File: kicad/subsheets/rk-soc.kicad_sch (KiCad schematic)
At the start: 1 part, among them U4 RK3566

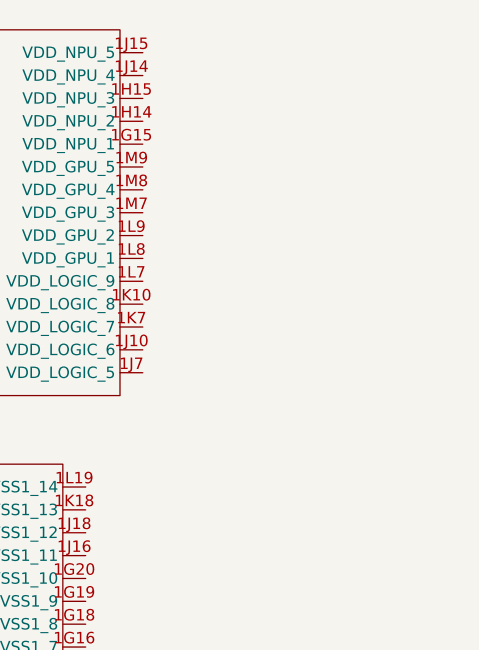
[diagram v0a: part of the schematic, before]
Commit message: Resize sheets
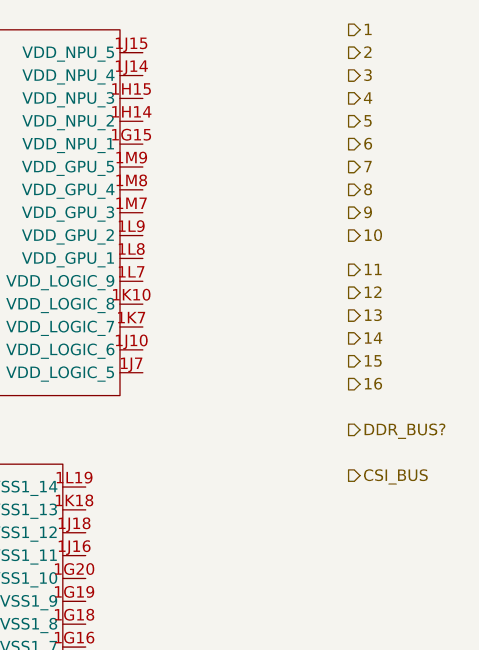
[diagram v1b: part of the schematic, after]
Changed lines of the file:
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@@
 	(generator_version "9.0")
 	(paper "A4")
+	(hierarchical_label "CSI_BUS"
+		(shape output)
+		(at 96.52 76.2 0)
+		(effects
+			(font
+				(size 1.27 1.27)
+			)
+			(justify left)
+		)
+	)
+	(hierarchical_label "16"
+		(shape output)
+		(at 96.52 66.04 0)
+		(effects
+			(font
+				(size 1.27 1.27)
+			)
+			(justify left)
+		)
+	)
+	(hierarchical_label "15"
+		(shape output)
+		(at 96.52 63.5 0)
+		(effects
+			(font
+				(size 1.27 1.27)
+			)
+			(justify left)
+		)
+	)
+	(hierarchical_label "10"
+		(shape output)
+		(at 96.52 49.53 0)
+		(effects
+			(font
+				(size 1.27 1.27)
+			)
+			(justify left)
+		)
+	)
+	(hierarchical_label "11"
+		(shape output)
+		(at 96.52 53.34 0)
+		(effects
+			(font
+				(size 1.27 1.27)
+			)
+			(justify left)
+		)
+	)
+	(hierarchical_label "12"
+		(shape output)
+		(at 96.52 55.88 0)
+		(effects
+			(font
+				(size 1.27 1.27)
+			)
+			(justify left)
+		)
+	)
+	(hierarchical_label "13"
+		(shape output)
+		(at 96.52 58.42 0)
+		(effects
+			(font
+				(size 1.27 1.27)
+			)
+			(justify left)
+		)
+	)
+	(hierarchical_label "14"
+		(shape output)
+		(at 96.52 60.96 0)
+		(effects
+			(font
+				(size 1.27 1.27)
+			)
+			(justify left)
+		)
+	)
+	(hierarchical_label "4"
+		(shape output)
+		(at 96.52 34.29 0)
+		(effects
+			(font
+				(size 1.27 1.27)
+			)
+			(justify left)
+		)
+	)
+	(hierarchical_label "3"
+		(shape output)
+		(at 96.52 31.75 0)
+		(effects
+			(font
+				(size 1.27 1.27)
+			)
+			(justify left)
+		)
+	)
+	(hierarchical_label "1"
+		(shape output)
+		(at 96.52 26.67 0)
+		(effects
+			(font
+				(size 1.27 1.27)
+			)
+			(justify left)
+		)
+	)
+	(hierarchical_label "2"
+		(shape output)
+		(at 96.52 29.21 0)
+		(effects
+			(font
+				(size 1.27 1.27)
+			)
+			(justify left)
+		)
+	)
+	(hierarchical_label "5"
+		(shape output)
+		(at 96.52 36.83 0)
+		(effects
+			(font
+				(size 1.27 1.27)
+			)
+			(justify left)
+		)
+	)
+	(hierarchical_label "6"
+		(shape output)
+		(at 96.52 39.37 0)
+		(effects
+			(font
+				(size 1.27 1.27)
+			)
+			(justify left)
+		)
+	)
+	(hierarchical_label "7"
+		(shape output)
+		(at 96.52 41.91 0)
+		(effects
+			(font
+				(size 1.27 1.27)
+			)
+			(justify left)
+		)
+	)
+	(hierarchical_label "8"
+		(shape output)
+		(at 96.52 44.45 0)
+		(effects
+			(font
+				(size 1.27 1.27)
+			)
+			(justify left)
+		)
+	)
+	(hierarchical_label "9"
+		(shape output)
+		(at 96.52 46.99 0)
+		(effects
+			(font
+				(size 1.27 1.27)
+			)
+			(justify left)
+		)
+	)
+	(hierarchical_label "DDR_BUS?"
+		(shape output)
+		(at 96.52 71.12 0)
+		(effects
+			(font
+				(size 1.27 1.27)
+			)
+			(justify left)
+		)
+	)
 	(symbol
 		(lib_id "RK35661_RK3566-altium-import:root_0_RK3566_")

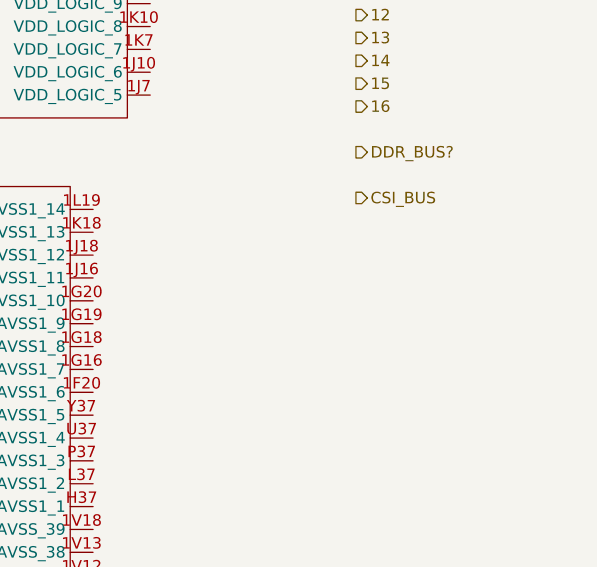
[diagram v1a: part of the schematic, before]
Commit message: Wire microsd port
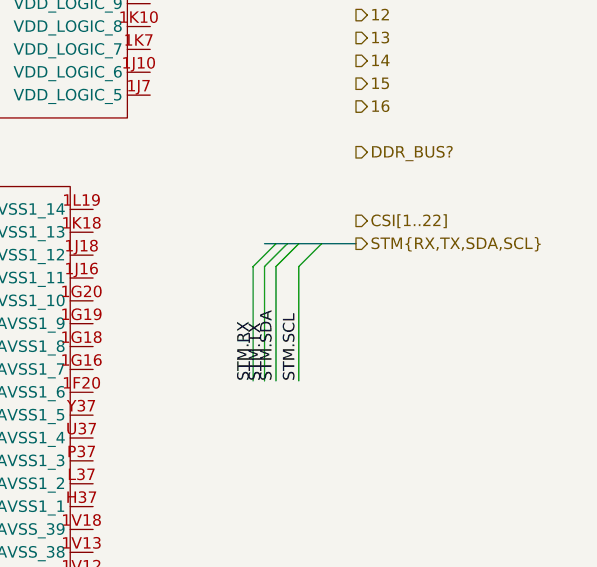
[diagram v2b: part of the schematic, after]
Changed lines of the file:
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@@
 	(generator_version "9.0")
 	(paper "A4")
-	(hierarchical_label "CSI_BUS"
-		(shape output)
-		(at 96.52 76.2 0)
+	(bus_entry
+		(at 92.71 81.28)
+		(size -2.54 2.54)
+		(stroke
+			(width 0)
+			(type default)
+		)
+	)
+	(bus_entry
+		(at 90.17 81.28)
+		(size -2.54 2.54)
+		(stroke
+			(width 0)
+			(type default)
+		)
+	)
+	(bus_entry
+		(at 87.63 81.28)
+		(size -2.54 2.54)
+		(stroke
+			(width 0)
+			(type default)
+		)
+	)
+	(bus_entry
+		(at 88.9 81.28)
+		(size -2.54 2.54)
+		(stroke
+			(width 0)
+			(type default)
+		)
+	)
+	(bus
+		(pts
+			(xy 92.71 81.28) (xy 96.52 81.28)
+		)
+		(stroke
+			(width 0)
+			(type default)
+		)
+	)
+	(wire
+		(pts
+			(xy 87.63 83.82) (xy 87.63 96.52)
+		)
+		(stroke
+			(width 0)
+			(type default)
+		)
+	)
+	(wire
+		(pts
+			(xy 85.09 83.82) (xy 85.09 96.52)
+		)
+		(stroke
+			(width 0)
+			(type default)
+		)
+	)
+	(bus
+		(pts
+			(xy 88.9 81.28) (xy 90.17 81.28)
+		)
+		(stroke
+			(width 0)
+			(type default)
+		)
+	)
+	(bus
+		(pts
+			(xy 86.36 81.28) (xy 87.63 81.28)
+		)
+		(stroke
+			(width 0)
+			(type default)
+		)
+	)
+	(bus
+		(pts
+			(xy 90.17 81.28) (xy 92.71 81.28)
+		)
+		(stroke
+			(width 0)
+			(type default)
+		)
+	)
+	(wire
+		(pts
+			(xy 86.36 83.82) (xy 86.36 96.52)
+		)
+		(stroke
+			(width 0)
+			(type default)
+		)
+	)
+	(wire
+		(pts
+			(xy 90.17 83.82) (xy 90.17 96.52)
+		)
+		(stroke
+			(width 0)
+			(type default)
+		)
+	)
+	(bus
+		(pts
+			(xy 87.63 81.28) (xy 88.9 81.28)
+		)
+		(stroke
+			(width 0)
+			(type default)
+		)
+	)
+	(label "STM.TX"
+		(at 86.36 96.52 90)
+		(effects
+			(font
+				(size 1.27 1.27)
+			)
+			(justify left bottom)
+		)
+	)
+	(label "STM.SDA"
+		(at 87.63 96.52 90)
+		(effects
+			(font
+				(size 1.27 1.27)
+			)
+			(justify left bottom)
+		)
+	)
+	(label "STM.SCL"
+		(at 90.17 96.52 90)
+		(effects
+			(font
+				(size 1.27 1.27)
+			)
+			(justify left bottom)
+		)
+	)
+	(label "STM.RX"
+		(at 85.09 96.52 90)
+		(effects
+			(font
+				(size 1.27 1.27)
+			)
+			(justify left bottom)
+		)
+	)
+	(hierarchical_label "CSI[1..22]"
+		(shape output)
+		(at 96.52 78.74 0)
+		(effects
+			(font
+				(size 1.27 1.27)
+			)
+			(justify left)
+		)
+	)
+	(hierarchical_label "5"
+		(shape output)
+		(at 96.52 36.83 0)
+		(effects
+			(font
+				(size 1.27 1.27)
+			)
+			(justify left)
+		)
+	)
+	(hierarchical_label "15"
+		(shape output)
+		(at 96.52 63.5 0)
 		(effects
 			(font
@@
 		)
 	)
-	(hierarchical_label "15"
-		(shape output)
-		(at 96.52 63.5 0)
+	(hierarchical_label "6"
+		(shape output)
+		(at 96.52 39.37 0)
+		(effects
+			(font
+				(size 1.27 1.27)
+			)
+			(justify left)
+		)
+	)
+	(hierarchical_label "9"
+		(shape output)
+		(at 96.52 46.99 0)
+		(effects
+			(font
+				(size 1.27 1.27)
+			)
+			(justify left)
+		)
+	)
+	(hierarchical_label "12"
+		(shape output)
+		(at 96.52 55.88 0)
+		(effects
+			(font
+				(size 1.27 1.27)
+			)
+			(justify left)
+		)
+	)
+	(hierarchical_label "3"
+		(shape output)
+		(at 96.52 31.75 0)
+		(effects
+			(font
+				(size 1.27 1.27)
+			)
+			(justify left)
+		)
+	)
+	(hierarchical_label "1"
+		(shape output)
+		(at 96.52 26.67 0)
+		(effects
+			(font
+				(size 1.27 1.27)
+			)
+			(justify left)
+		)
+	)
+	(hierarchical_label "11"
+		(shape output)
+		(at 96.52 53.34 0)
 		(effects
 			(font
@@
 		)
 	)
-	(hierarchical_label "11"
-		(shape output)
-		(at 96.52 53.34 0)
-		(effects
-			(font
-				(size 1.27 1.27)
-			)
-			(justify left)
-		)
-	)
-	(hierarchical_label "12"
-		(shape output)
-		(at 96.52 55.88 0)
+	(hierarchical_label "4"
+		(shape output)
+		(at 96.52 34.29 0)
 		(effects
 			(font
@@
 		)
 	)
+	(hierarchical_label "8"
+		(shape output)
+		(at 96.52 44.45 0)
+		(effects
+			(font
+				(size 1.27 1.27)
+			)
+			(justify left)
+		)
+	)
+	(hierarchical_label "DDR_BUS?"
+		(shape output)
+		(at 96.52 71.12 0)
+		(effects
+			(font
+				(size 1.27 1.27)
+			)
+			(justify left)
+		)
+	)
 	(hierarchical_label "14"
 		(shape output)
@@
 		)
 	)
-	(hierarchical_label "4"
-		(shape output)
-		(at 96.52 34.29 0)
-		(effects
-			(font
-				(size 1.27 1.27)
-			)
-			(justify left)
-		)
-	)
-	(hierarchical_label "3"
-		(shape output)
-		(at 96.52 31.75 0)
-		(effects
-			(font
-				(size 1.27 1.27)
-			)
-			(justify left)
-		)
-	)
-	(hierarchical_label "1"
-		(shape output)
-		(at 96.52 26.67 0)
+	(hierarchical_label "STM{RX,TX,SDA,SCL}"
+		(shape output)
+		(at 96.52 81.28 0)
+		(effects
+			(font
+				(size 1.27 1.27)
+			)
+			(justify left)
+		)
+	)
+	(hierarchical_label "7"
+		(shape output)
+		(at 96.52 41.91 0)
 		(effects
 			(font
@@
 		(effects
 			(font
-				(size 1.27 1.27)
-			)
-			(justify left)
-		)
-	)
-	(hierarchical_label "5"
-		(shape output)
-		(at 96.52 36.83 0)
-		(effects
-			(font
-				(size 1.27 1.27)
-			)
-			(justify left)
-		)
-	)
-	(hierarchical_label "6"
-		(shape output)
-		(at 96.52 39.37 0)
-		(effects
-			(font
-				(size 1.27 1.27)
-			)
-			(justify left)
-		)
-	)
-	(hierarchical_label "7"
-		(shape output)
-		(at 96.52 41.91 0)
-		(effects
-			(font
-				(size 1.27 1.27)
-			)
-			(justify left)
-		)
-	)
-	(hierarchical_label "8"
-		(shape output)
-		(at 96.52 44.45 0)
-		(effects
-			(font
-				(size 1.27 1.27)
-			)
-			(justify left)
-		)
-	)
-	(hierarchical_label "9"
-		(shape output)
-		(at 96.52 46.99 0)
-		(effects
-			(font
-				(size 1.27 1.27)
-			)
-			(justify left)
-		)
-	)
-	(hierarchical_label "DDR_BUS?"
-		(shape output)
-		(at 96.52 71.12 0)
-		(effects
-			(font
